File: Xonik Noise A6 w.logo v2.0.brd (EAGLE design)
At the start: 29.8 x 26 mm, 38 parts, among them IC1 TL074D, T1 NOISE-2N3904

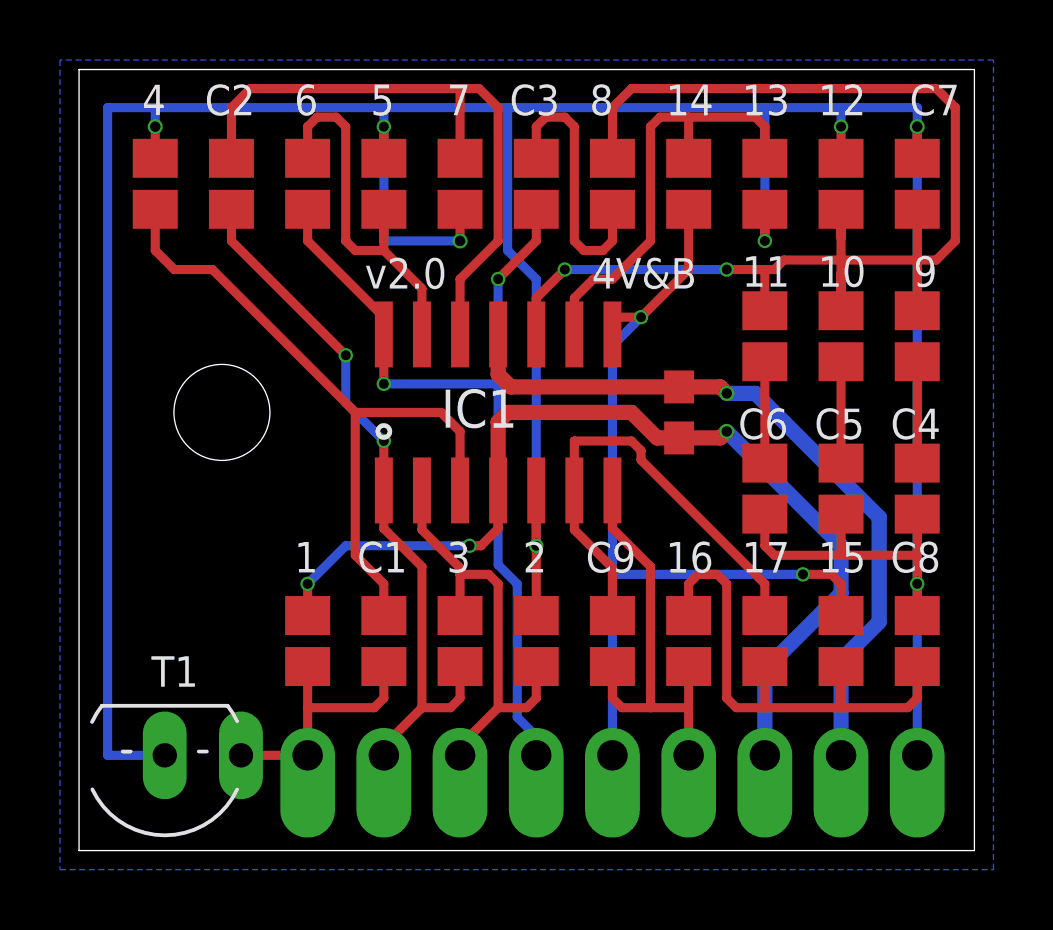
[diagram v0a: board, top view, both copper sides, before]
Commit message: Removed default gain resistor and added doc for trimmer
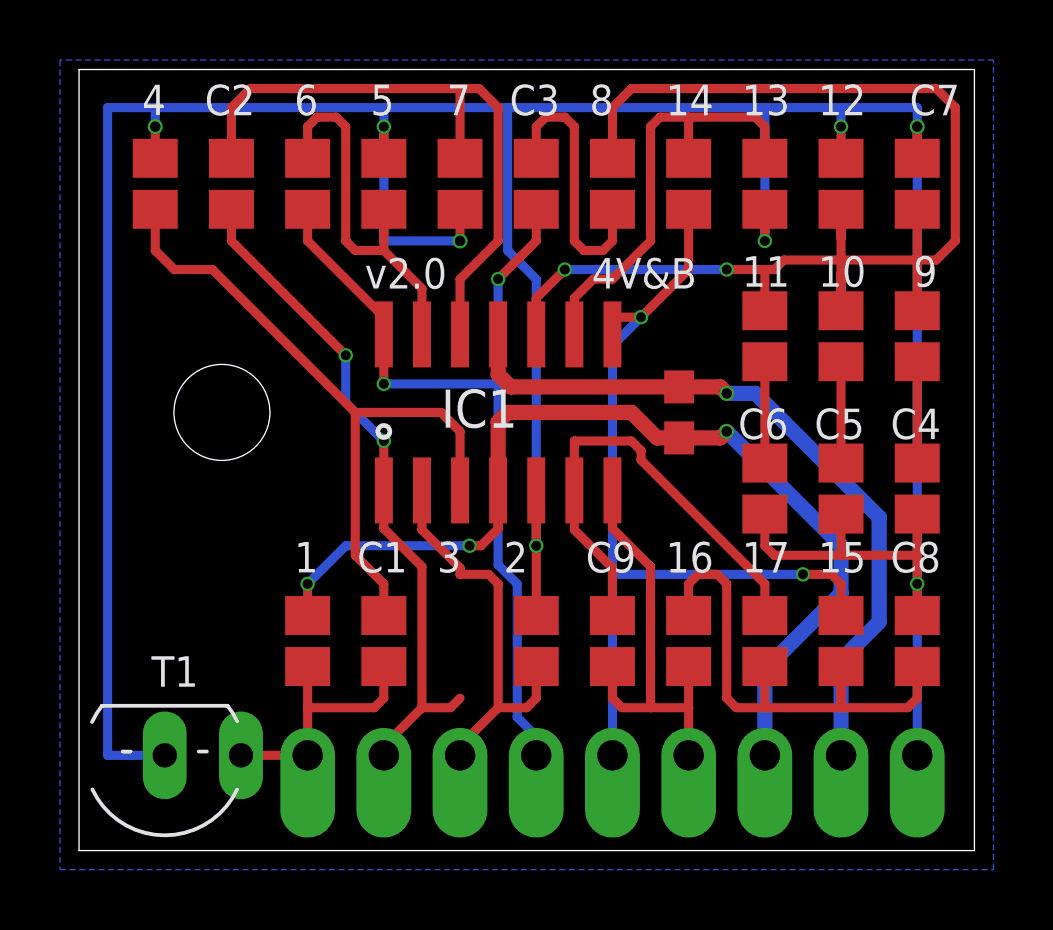
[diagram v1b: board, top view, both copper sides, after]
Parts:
- removed 3: 20k, resistor:R0805
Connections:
- net N$1: no longer 3.2
- net N$9: no longer 3.1
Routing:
- net N$1: track 15.1 -> 13.5 mm
- net N$9: track 23.8 -> 22.8 mm
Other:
- board text added: "50k Trim"
- board text added: "AGND"
- board text removed: "Gnd"
- board text removed: "Trim"
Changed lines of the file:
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@@
 <grid distance="0.0125" unitdist="inch" unit="mm" style="dots" multiple="1" display="yes" altdistance="0.025" altunitdist="inch" altunit="inch"/>
 <layers>
-<layer number="1" name="Top" color="4" fill="1" visible="yes" active="yes"/>
+<layer number="1" name="Top" color="4" fill="1" visible="no" active="yes"/>
 <layer number="2" name="Route2" color="1" fill="3" visible="no" active="no"/>
 <layer number="3" name="Route3" color="4" fill="3" visible="no" active="no"/>
@@
 <layer number="19" name="Unrouted" color="6" fill="1" visible="yes" active="yes"/>
 <layer number="20" name="Dimension" color="15" fill="1" visible="yes" active="yes"/>
-<layer number="21" name="tPlace" color="7" fill="1" visible="yes" active="yes"/>
+<layer number="21" name="tPlace" color="7" fill="1" visible="no" active="yes"/>
 <layer number="22" name="bPlace" color="7" fill="1" visible="yes" active="yes"/>
-<layer number="23" name="tOrigins" color="15" fill="1" visible="yes" active="yes"/>
+<layer number="23" name="tOrigins" color="15" fill="1" visible="no" active="yes"/>
 <layer number="24" name="bOrigins" color="15" fill="1" visible="yes" active="yes"/>
-<layer number="25" name="tNames" color="7" fill="1" visible="yes" active="yes"/>
+<layer number="25" name="tNames" color="7" fill="1" visible="no" active="yes"/>
 <layer number="26" name="bNames" color="7" fill="1" visible="yes" active="yes"/>
 <layer number="27" name="tValues" color="7" fill="1" visible="no" active="yes"/>
@@
 <layer number="37" name="tTest" color="7" fill="1" visible="no" active="yes"/>
 <layer number="38" name="bTest" color="7" fill="1" visible="no" active="yes"/>
-<layer number="39" name="tKeepout" color="4" fill="11" visible="yes" active="yes"/>
+<layer number="39" name="tKeepout" color="4" fill="11" visible="no" active="yes"/>
 <layer number="40" name="bKeepout" color="1" fill="11" visible="yes" active="yes"/>
-<layer number="41" name="tRestrict" color="4" fill="10" visible="yes" active="yes"/>
+<layer number="41" name="tRestrict" color="4" fill="10" visible="no" active="yes"/>
 <layer number="42" name="bRestrict" color="1" fill="10" visible="yes" active="yes"/>
 <layer number="43" name="vRestrict" color="2" fill="10" visible="no" active="yes"/>
@@
 <layer number="49" name="Reference" color="7" fill="1" visible="no" active="yes"/>
 <layer number="50" name="dxf" color="7" fill="1" visible="no" active="no"/>
-<layer number="51" name="tDocu" color="7" fill="1" visible="yes" active="yes"/>
+<layer number="51" name="tDocu" color="7" fill="1" visible="no" active="yes"/>
 <layer number="52" name="bDocu" color="7" fill="1" visible="yes" active="yes"/>
 <layer number="53" name="tGND_GNDA" color="7" fill="9" visible="no" active="no"/>
@@
 <wire x1="0" y1="26.035" x2="0" y2="0" width="0" layer="20"/>
 <text x="6.985" y="5.715" size="1.016" layer="26" rot="MR90">In</text>
-<text x="9.525" y="5.715" size="1.016" layer="26" rot="MR90">Trim</text>
-<text x="12.065" y="5.715" size="1.016" layer="26" rot="MR90">Trim</text>
+<text x="10.16" y="6.35" size="1.016" layer="26" rot="MR90">50k
+Trim</text>
 <text x="14.605" y="5.715" size="1.016" layer="26" rot="MR90">White</text>
 <text x="17.145" y="5.715" size="1.016" layer="26" rot="MR90">Pink</text>
@@
 <text x="22.225" y="5.715" size="1.016" layer="26" rot="MR90">+15V</text>
 <text x="24.765" y="5.715" size="1.016" layer="26" rot="MR90">-15V</text>
-<text x="27.305" y="5.715" size="1.016" layer="26" rot="MR90">Gnd</text>
+<text x="27.305" y="5.715" size="1.016" layer="26" rot="MR90">AGND</text>
 <circle x="10.16" y="13.97" radius="0.0762" width="0.4064" layer="25"/>
 <text x="7.1755" y="9.271" size="1.016" layer="25">1</text>
-<text x="14.7955" y="9.271" size="1.016" layer="25">2</text>
-<text x="12.2555" y="9.271" size="1.016" layer="25">3</text>
+<text x="14.1605" y="9.271" size="1.016" layer="25">2</text>
+<text x="11.938" y="9.271" size="1.016" layer="25">3</text>
 <text x="2.0955" y="24.511" size="1.016" layer="25">4</text>
 <text x="9.7155" y="24.511" size="1.016" layer="25">5</text>
@@
 <vertex x="22.362696875" y="20.173490625"/>
 </polygon>
+<wire x1="13.335" y1="5.715" x2="9.2075" y2="5.715" width="0.1" layer="26"/>
+<wire x1="9.2075" y1="5.715" x2="9.2075" y2="4.7625" width="0.1" layer="26"/>
+<wire x1="13.335" y1="5.715" x2="13.335" y2="4.7625" width="0.1" layer="26"/>
 </plain>
 <attributes>
@@
 <attribute name="VALUE" x="17.526" y="6.223" size="1.27" layer="27" rot="R90"/>
 </element>
-<element name="3" library="resistor" package="R0805" value="20k" x="12.7" y="6.985" smashed="yes" rot="R90">
-<attribute name="VALUE" x="14.986" y="6.223" size="1.27" layer="27" rot="R90"/>
-</element>
 <element name="4" library="resistor" package="R0805" value="100k" x="2.54" y="22.225" smashed="yes" rot="R90">
 <attribute name="VALUE" x="4.826" y="21.463" size="1.27" layer="27" rot="R90"/>
@@
 <signal name="N$1">
 <contactref element="2" pad="1"/>
-<contactref element="3" pad="2"/>
 <contactref element="IC1" pad="2"/>
 <contactref element="LEVEL1" pad="1"/>
 <wire x1="11.43" y1="12.005" x2="11.43" y2="10.6925" width="0.3048" layer="1"/>
-<wire x1="12.7" y1="7.835" x2="12.7" y2="9.2075" width="0.3048" layer="1"/>
 <wire x1="12.7" y1="9.2075" x2="12.7" y2="9.4225" width="0.3048" layer="1"/>
 <wire x1="12.7" y1="9.4225" x2="11.43" y2="10.6925" width="0.3048" layer="1"/>
-<wire x1="12.7" y1="7.835" x2="12.7" y2="7.62" width="0.3048" layer="1"/>
 <wire x1="15.24" y1="6.135" x2="15.24" y2="6.0575125" width="0.3048" layer="1"/>
 <wire x1="12.7" y1="3.175" x2="12.7" y2="3.4925" width="0.3048" layer="1"/>
@@
 </signal>
 <signal name="N$9">
-<contactref element="3" pad="1"/>
 <contactref element="IC1" pad="1"/>
 <contactref element="LEVEL2" pad="1"/>
@@
 <wire x1="8.89" y1="16.51" x2="5.08" y2="20.32" width="0.3048" layer="1"/>
 <wire x1="5.08" y1="20.32" x2="5.08" y2="21.375" width="0.3048" layer="1"/>
-<wire x1="12.7" y1="6.135" x2="12.7" y2="5.08" width="0.3048" layer="1"/>
 <wire x1="12.7" y1="5.08" x2="12.3825" y2="4.7625" width="0.3048" layer="1"/>
 <wire x1="12.3825" y1="4.7625" x2="11.43" y2="4.7625" width="0.3048" layer="1"/>
@@
 </board>
 </drawing>
+<compatibility>
+<note version="6.3" minversion="6.2.2" severity="warning">
+Since Version 6.2.2 text objects can contain more than one line,
+which will not be processed correctly with this version.
+</note>
+</compatibility>
 </eagle>

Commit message: Changed to logo-as-component
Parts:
- added U$1: (no value), joakim:XONIK_LOGO_18

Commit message: Added working bom and gerber
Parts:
- 17: value 301k -> 300k
- 9: value 33.2k -> 33k
- C10: value (none) -> 100nF
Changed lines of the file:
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@@
 <attribute name="VALUE" x="15.494" y="22.987" size="1.27" layer="27" rot="R270"/>
 </element>
-<element name="9" library="resistor" package="R0805" value="33.2k" x="27.94" y="17.145" smashed="yes" rot="R270">
+<element name="9" library="resistor" package="R0805" value="33k" x="27.94" y="17.145" smashed="yes" rot="R270">
 <attribute name="VALUE" x="25.654" y="17.907" size="1.27" layer="27" rot="R270"/>
 </element>
@@
 <attribute name="VALUE" x="18.034" y="7.747" size="1.27" layer="27" rot="R270"/>
 </element>
-<element name="17" library="resistor" package="R0805" value="301k" x="22.86" y="6.985" smashed="yes" rot="R90">
+<element name="17" library="resistor" package="R0805" value="300k" x="22.86" y="6.985" smashed="yes" rot="R90">
 <attribute name="VALUE" x="25.146" y="6.223" size="1.27" layer="27" rot="R90"/>
 </element>
@@
 <attribute name="VALUE" x="19.812" y="12.7" size="1.27" layer="27" rot="R90"/>
 </element>
-<element name="C10" library="resistor" package="C0603" value="" x="20.0025" y="14.605" smashed="yes" rot="R270">
+<element name="C10" library="resistor" package="C0603" value="100nF" x="20.0025" y="14.605" smashed="yes" rot="R270">
 <attribute name="VALUE" x="17.9705" y="15.494" size="1.27" layer="27" rot="R270"/>
 </element>
